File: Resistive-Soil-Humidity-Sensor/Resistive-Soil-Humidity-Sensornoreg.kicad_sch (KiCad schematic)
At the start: 9 parts, among them Q1 BC547, U1 L7805CV

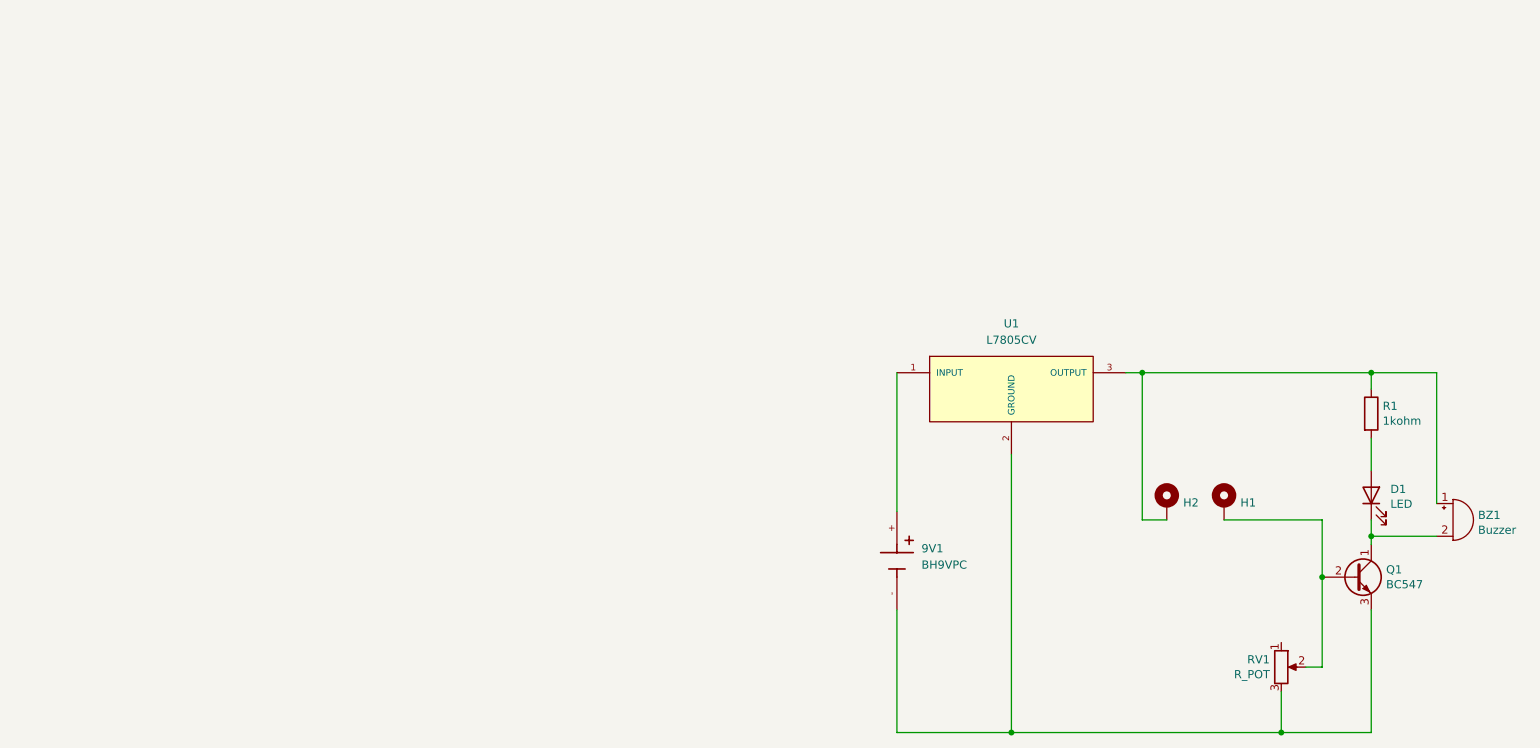
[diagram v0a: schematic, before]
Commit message: added buzzer
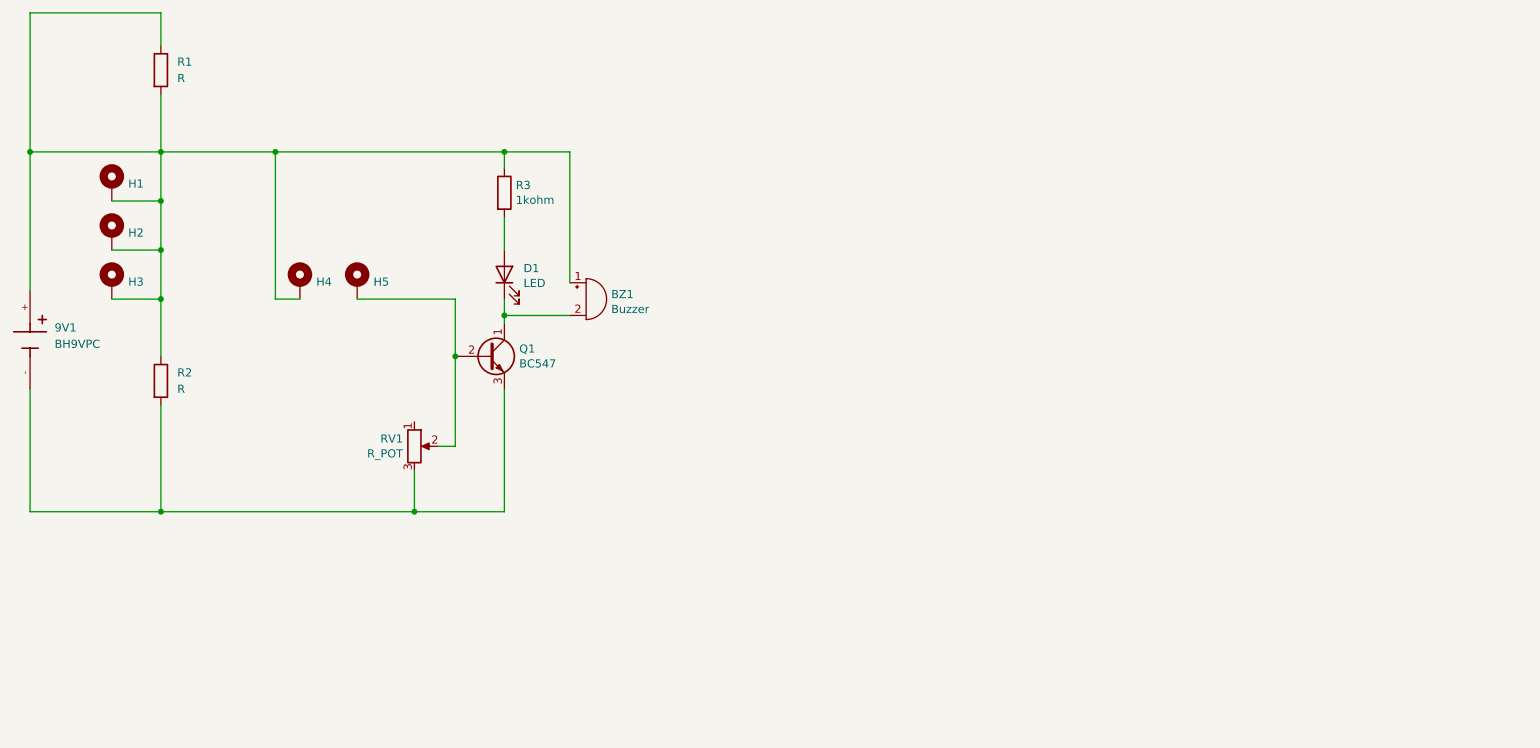
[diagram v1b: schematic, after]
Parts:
- removed U1: L7805CV, TO255P1040X460X1968-3, symbol L7805CV:L7805CV
- added H3, H4, H5: MountingHole_Pad, Connector_Pin:Pin_D0.9mm_L10.0mm_W2.4mm_FlatFork, symbol Mechanical:MountingHole_Pad
- added R2: R, Resistor_THT:R_Axial_DIN0204_L3.6mm_D1.6mm_P5.08mm_Horizontal, symbol Device:R
- added R3: 1kohm, Resistor_SMD:R_0402_1005Metric, symbol Device:R
- R1: value 1kohm -> R; footprint Resistor_SMD:R_0402_1005Metric -> Resistor_THT:R_Axial_DIN0204_L3.6mm_D1.6mm_P5.08mm_Horizontal
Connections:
- net at Q1.2 (B), RV1.2: now also H5.1; no longer H1.1
- net at 9V1.-, Q1.3 (E), RV1.3: now also R2.2
- net at R1.2: now also 9V1.+, BZ1.1 (-), H1.1, H2.1, R1.1, H3.1, H4.1, R2.1, R3.1; no longer D1.2 (A)
- new net: D1.2 (A), R3.2
